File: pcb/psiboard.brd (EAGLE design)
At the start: 205.7 x 111.8 mm, 4 parts

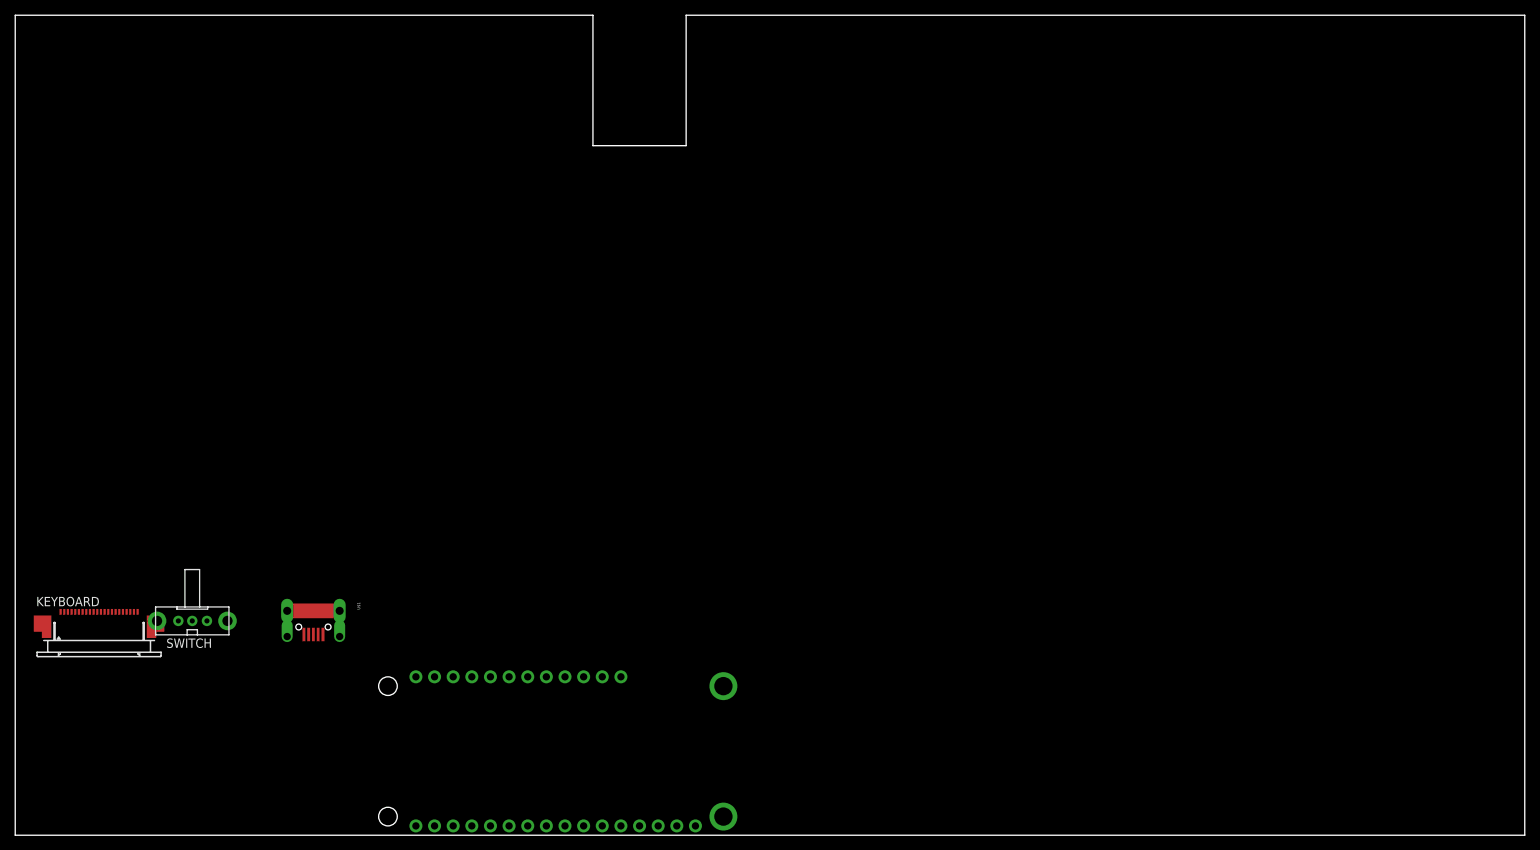
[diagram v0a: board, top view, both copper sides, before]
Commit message: Starting to get to the correct board shape.
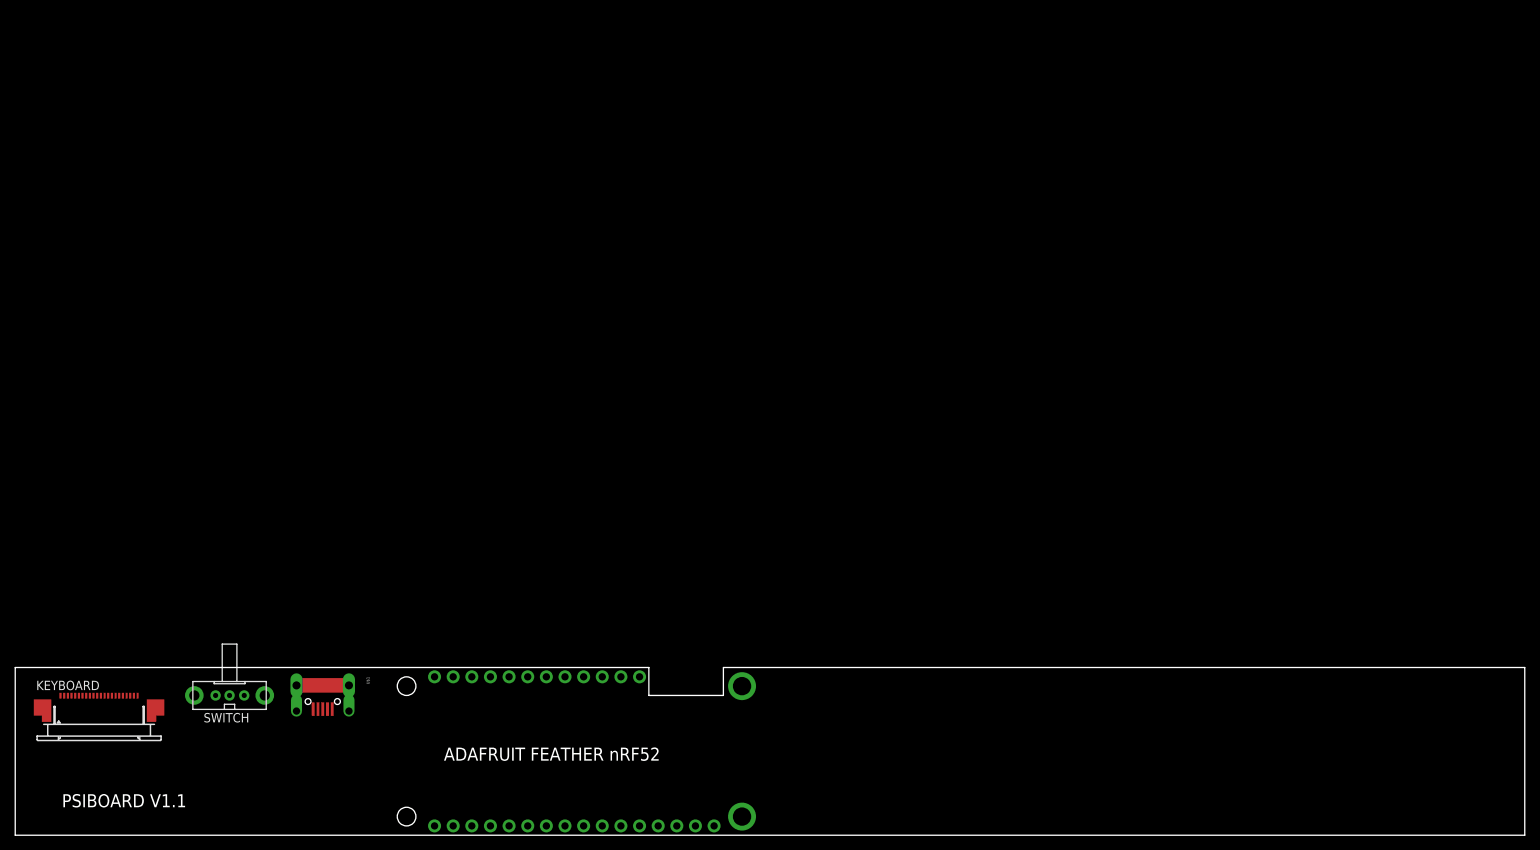
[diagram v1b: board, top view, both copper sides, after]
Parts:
- moved KEYBOARD 11.4 mm to (11.4, 16.5)
- moved SWITCH 11.4 mm to (29.2, 19.1)
- moved U$1 10.2 mm to (41.9, 20.3)
- moved FEATHER 2.54 mm to (101.6, 0.00)
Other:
- board size 205.7 x 111.8 mm -> 205.7 x 22.9 mm
- board text added: "ADAFRUIT FEATHER nRF52"
- board text added: "PSIBOARD V1.1"
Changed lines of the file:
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@@
 <plain>
 <wire x1="0" y1="0" x2="205.74" y2="0" width="0.1524" layer="20"/>
-<wire x1="205.74" y1="0" x2="205.74" y2="111.76" width="0.1524" layer="20"/>
-<wire x1="205.74" y1="111.76" x2="91.44" y2="111.76" width="0.1524" layer="20"/>
-<wire x1="91.44" y1="111.76" x2="91.44" y2="93.98" width="0.1524" layer="20"/>
-<wire x1="91.44" y1="93.98" x2="78.74" y2="93.98" width="0.1524" layer="20"/>
-<wire x1="78.74" y1="93.98" x2="78.74" y2="111.76" width="0.1524" layer="20"/>
-<wire x1="78.74" y1="111.76" x2="0" y2="111.76" width="0.1524" layer="20"/>
-<wire x1="0" y1="111.76" x2="0" y2="0" width="0.1524" layer="20"/>
+<wire x1="205.74" y1="0" x2="205.74" y2="22.86" width="0.1524" layer="20"/>
+<wire x1="205.74" y1="22.86" x2="96.52" y2="22.86" width="0.1524" layer="20"/>
+<wire x1="96.52" y1="22.86" x2="96.52" y2="19.05" width="0.1524" layer="20"/>
+<wire x1="96.52" y1="19.05" x2="86.36" y2="19.05" width="0.1524" layer="20"/>
+<wire x1="86.36" y1="19.05" x2="86.36" y2="22.86" width="0.1524" layer="20"/>
+<wire x1="86.36" y1="22.86" x2="0" y2="22.86" width="0.1524" layer="20"/>
+<wire x1="0" y1="22.86" x2="0" y2="0" width="0.1524" layer="20"/>
+<text x="6.35" y="3.81" size="1.778" layer="20">PSIBOARD V1.1</text>
+<text x="58.42" y="10.16" size="1.778" layer="20">ADAFRUIT FEATHER nRF52</text>
 </plain>
 <attributes>
@@
 </autorouter>
 <elements>
-<element name="FEATHER" library="adafruit" library_urn="urn:adsk.eagle:library:420" package="FEATHERWING_DIM" value="FEATHERWING_NODIM" x="99.06" y="0" rot="MR0"/>
-<element name="KEYBOARD" library="con-molex" library_urn="urn:adsk.eagle:library:165" package="52745-2290" value="52745-2290" x="11.43" y="27.94">
-<attribute name="MF" value="MOLEX" x="11.43" y="27.94" size="1.778" layer="27" display="off"/>
-<attribute name="MPN" value="" x="11.43" y="27.94" size="1.778" layer="27" display="off"/>
-<attribute name="OC_FARNELL" value="unknown" x="11.43" y="27.94" size="1.778" layer="27" display="off"/>
-<attribute name="OC_NEWARK" value="unknown" x="11.43" y="27.94" size="1.778" layer="27" display="off"/>
+<element name="FEATHER" library="adafruit" library_urn="urn:adsk.eagle:library:420" package="FEATHERWING_DIM" value="FEATHERWING_NODIM" x="101.6" y="0" rot="MR0"/>
+<element name="KEYBOARD" library="con-molex" library_urn="urn:adsk.eagle:library:165" package="52745-2290" value="52745-2290" x="11.43" y="16.51">
+<attribute name="MF" value="MOLEX" x="11.43" y="16.51" size="1.778" layer="27" display="off"/>
+<attribute name="MPN" value="" x="11.43" y="16.51" size="1.778" layer="27" display="off"/>
+<attribute name="OC_FARNELL" value="unknown" x="11.43" y="16.51" size="1.778" layer="27" display="off"/>
+<attribute name="OC_NEWARK" value="unknown" x="11.43" y="16.51" size="1.778" layer="27" display="off"/>
 </element>
-<element name="SWITCH" library="adafruit" library_urn="urn:adsk.eagle:library:420" package="EG1213" value="EG1213" x="24.13" y="29.21" rot="R180"/>
-<element name="U$1" library="micro usb B - 4LEGS" package="MICRO_USB_4_LEGS" value="MICRO-USB-B" x="40.64" y="30.48" rot="R270"/>
+<element name="SWITCH" library="adafruit" library_urn="urn:adsk.eagle:library:420" package="EG1213" value="EG1213" x="29.21" y="19.05" rot="R180"/>
+<element name="U$1" library="micro usb B - 4LEGS" package="MICRO_USB_4_LEGS" value="MICRO-USB-B" x="41.91" y="20.32" rot="R270"/>
 </elements>
 <signals>
@@
 <contactref element="FEATHER" pad="26"/>
 <contactref element="U$1" pad="VCC"/>
-<wire x1="77.47" y1="21.59" x2="41.94" y2="27.355" width="0" layer="19" extent="1-1"/>
+<wire x1="80.01" y1="21.59" x2="43.21" y2="17.195" width="0" layer="19" extent="1-1"/>
 </signal>
 <signal name="EN">
 <contactref element="FEATHER" pad="27"/>
 <contactref element="SWITCH" pad="2"/>
-<wire x1="24.13" y1="29.21" x2="80.01" y2="21.59" width="0" layer="19" extent="1-1"/>
+<wire x1="29.21" y1="19.05" x2="82.55" y2="21.59" width="0" layer="19" extent="1-1"/>
 </signal>
 <signal name="6">
@@
 <contactref element="KEYBOARD" pad="22"/>
 <contactref element="U$1" pad="GND" route="any" routetag="G$1.GND"/>
-<wire x1="85.09" y1="1.27" x2="39.34" y2="27.355" width="0" layer="19" extent="1-1"/>
-<wire x1="6.18" y1="30.44" x2="85.09" y2="1.27" width="0" layer="19" extent="1-1"/>
-<wire x1="16.68" y1="30.44" x2="6.18" y2="30.44" width="0" layer="19" extent="1-1"/>
-<wire x1="22.23" y1="29.21" x2="16.68" y2="30.44" width="0" layer="19" extent="1-1"/>
+<wire x1="87.63" y1="1.27" x2="40.61" y2="17.195" width="0" layer="19" extent="1-1"/>
+<wire x1="6.18" y1="19.01" x2="87.63" y2="1.27" width="0" layer="19" extent="1-1"/>
+<wire x1="16.68" y1="19.01" x2="6.18" y2="19.01" width="0" layer="19" extent="1-1"/>
+<wire x1="27.31" y1="19.05" x2="16.68" y2="19.01" width="0" layer="19" extent="1-1"/>
 </signal>
 <signal name="2">
@@
 <contactref element="KEYBOARD" pad="2"/>
 <contactref element="KEYBOARD" pad="5"/>
-<wire x1="8.18" y1="30.44" x2="6.68" y2="30.44" width="0" layer="19" extent="1-1"/>
+<wire x1="8.18" y1="19.01" x2="6.68" y2="19.01" width="0" layer="19" extent="1-1"/>
 </signal>
 </signals>

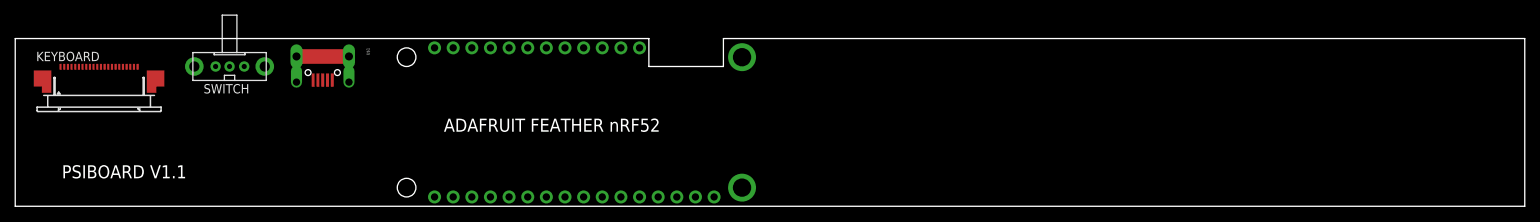
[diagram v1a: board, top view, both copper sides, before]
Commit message: Basic board layout now complete, including silkscreen names.
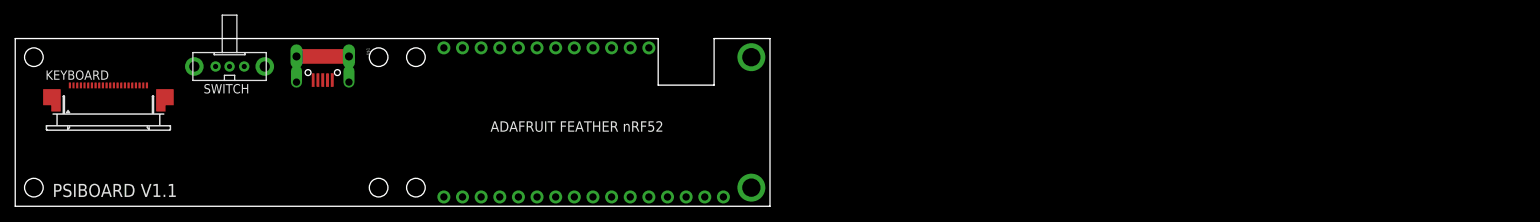
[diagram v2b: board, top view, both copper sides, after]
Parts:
- moved KEYBOARD 2.84 mm to (12.7, 14.0)
- moved FEATHER 1.27 mm to (102.9, 0.00)
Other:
- board size 205.7 x 22.9 mm -> 102.9 x 22.9 mm
